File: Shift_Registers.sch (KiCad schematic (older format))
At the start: 3 parts

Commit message: Finished draft schema
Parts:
- added J1: SPARE, symbol Connector:Conn_01x03_Female
- added U17: 74HC595, symbol 74xx:74HC595
- gave numbers to parts that had none: 3
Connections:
- net 5V: now also U17.10 (~SRCLR), U17.16 (VCC)
- net BLANK: now also U17.13 (~OE)
- net GND: now also J1.3 (Pin_3), U17.8 (GND)
- net SHIFTCLK: now also U17.11 (SRCLK)
- net STORAGECLK: now also U17.12 (RCLK)
- net at U16.9 (QH'): now also U17.14 (SER)
- new net: J1.1 (Pin_1), U17.6 (QG)
- new net: J1.2 (Pin_2), U17.7 (QH)
- new net DP1: U17.15 (QA)
- new net DP2: U17.1 (QB)
- new net DP3: U17.2 (QC)
- new net DP4: U17.3 (QD)
- new net DP5: U17.4 (QE)
- new net DP6: U17.5 (QF)
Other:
- moved on the sheet: U14, U15, U16

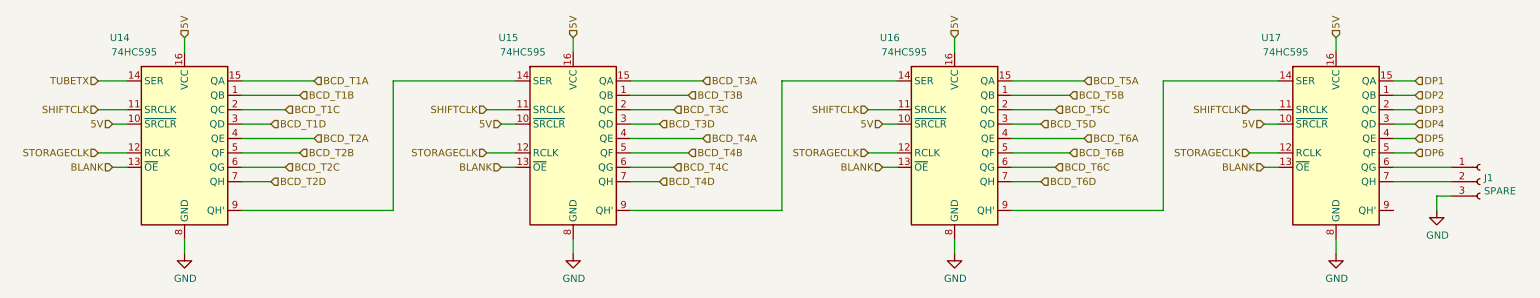
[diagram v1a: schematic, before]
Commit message: Finished schema and started PCB layout
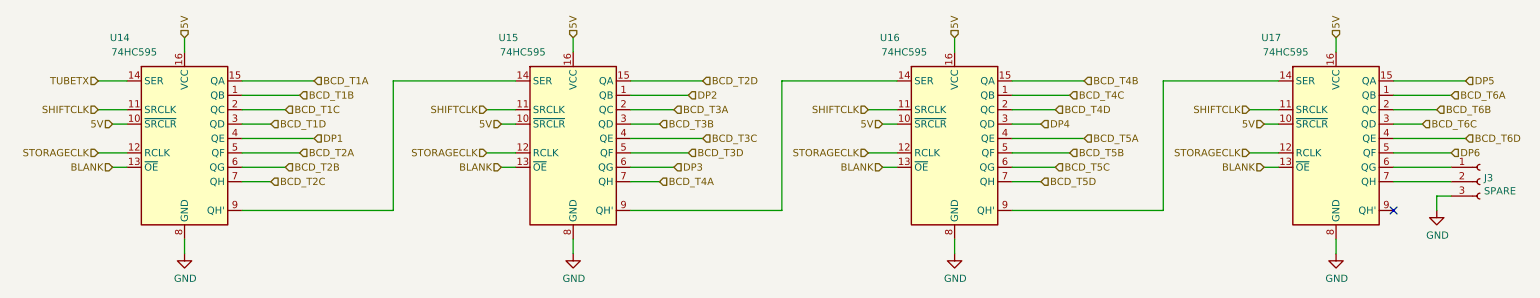
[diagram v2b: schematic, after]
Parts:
- J3: renamed from J1; footprint (none) -> Connector_PinHeader_2.54mm:PinHeader_1x03_P2.54mm_Vertical
- U14, U15, U16, U17: footprint (none) -> Package_SO:SOIC-16_3.9x9.9mm_P1.27mm
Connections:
- net BCD_T2A: now also U14.5 (QF); no longer U14.4 (QE)
- net BCD_T2B: now also U14.6 (QG); no longer U14.5 (QF)
- net BCD_T2C: now also U14.7 (QH); no longer U14.6 (QG)
- net BCD_T2D: now also U15.15 (QA); no longer U14.7 (QH)
- net BCD_T3A: now also U15.2 (QC); no longer U15.15 (QA)
- net BCD_T3B: now also U15.3 (QD); no longer U15.1 (QB)
- net BCD_T3C: now also U15.4 (QE); no longer U15.2 (QC)
- net BCD_T3D: now also U15.5 (QF); no longer U15.3 (QD)
- net BCD_T4A: now also U15.7 (QH); no longer U15.4 (QE)
- net BCD_T4B: now also U16.15 (QA); no longer U15.5 (QF)
- net BCD_T4C: now also U16.1 (QB); no longer U15.6 (QG)
- net BCD_T4D: now also U16.2 (QC); no longer U15.7 (QH)
- net BCD_T5A: now also U16.4 (QE); no longer U16.15 (QA)
- net BCD_T5B: now also U16.5 (QF); no longer U16.1 (QB)
- net BCD_T5C: now also U16.6 (QG); no longer U16.2 (QC)
- net BCD_T5D: now also U16.7 (QH); no longer U16.3 (QD)
- net BCD_T6A: now also U17.1 (QB); no longer U16.4 (QE)
- net BCD_T6B: now also U17.2 (QC); no longer U16.5 (QF)
- net BCD_T6C: now also U17.3 (QD); no longer U16.6 (QG)
- net BCD_T6D: now also U17.4 (QE); no longer U16.7 (QH)
- net DP1: now also U14.4 (QE); no longer U17.15 (QA)
- net DP2: now also U15.1 (QB); no longer U17.1 (QB)
- net DP3: now also U15.6 (QG); no longer U17.2 (QC)
- net DP4: now also U16.3 (QD); no longer U17.3 (QD)
- net DP5: now also U17.15 (QA); no longer U17.4 (QE)
- no-connect marks 0 -> 1
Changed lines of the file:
@@
 Comment4 ""
 $EndDescr
+Text HLabel 10600 3300 2    50   Input ~ 0
+BCD_T6A
+Text HLabel 10500 3400 2    50   Input ~ 0
+BCD_T6B
+Text HLabel 10400 3500 2    50   Input ~ 0
+BCD_T6C
 Text HLabel 8050 3600 2    50   Input ~ 0
-BCD_T6A
+BCD_T5A
 Text HLabel 7950 3700 2    50   Input ~ 0
-BCD_T6B
+BCD_T5B
 Text HLabel 7850 3800 2    50   Input ~ 0
-BCD_T6C
+BCD_T5C
+Text HLabel 7750 3900 2    50   Input ~ 0
+BCD_T5D
+Text HLabel 5100 3900 2    50   Input ~ 0
+BCD_T4A
 Text HLabel 8050 3200 2    50   Input ~ 0
-BCD_T5A
+BCD_T4B
 Text HLabel 7950 3300 2    50   Input ~ 0
-BCD_T5B
+BCD_T4C
 Text HLabel 7850 3400 2    50   Input ~ 0
-BCD_T5C
-Text HLabel 7750 3500 2    50   Input ~ 0
-BCD_T5D
-Text HLabel 5400 3600 2    50   Input ~ 0
-BCD_T4A
-Text HLabel 5300 3700 2    50   Input ~ 0
-BCD_T4B
-Text HLabel 5200 3800 2    50   Input ~ 0
-BCD_T4C
-Text HLabel 5100 3900 2    50   Input ~ 0
 BCD_T4D
-Text HLabel 7750 3900 2    50   Input ~ 0
+Text HLabel 10700 3600 2    50   Input ~ 0
 BCD_T6D
 Text HLabel 2500 3400 2    50   Input ~ 0
 BCD_T1C
-Text HLabel 2700 3600 2    50   Input ~ 0
+Text HLabel 2600 3700 2    50   Input ~ 0
 BCD_T2A
-Text HLabel 2500 3800 2    50   Input ~ 0
+Text HLabel 2400 3900 2    50   Input ~ 0
 BCD_T2C
-Text HLabel 5400 3200 2    50   Input ~ 0
+Text HLabel 5200 3400 2    50   Input ~ 0
 BCD_T3A
-Text HLabel 5300 3300 2    50   Input ~ 0
+Text HLabel 5100 3500 2    50   Input ~ 0
 BCD_T3B
-Text HLabel 5200 3400 2    50   Input ~ 0
+Text HLabel 5400 3600 2    50   Input ~ 0
 BCD_T3C
-Text HLabel 5100 3500 2    50   Input ~ 0
+Text HLabel 5300 3700 2    50   Input ~ 0
 BCD_T3D
 $Comp
@@
 F 0 "U14" H 1350 4300 50  0000 C CNN
 F 1 "74HC595" H 1450 4200 50  0000 C CNN
-F 2 "" H 1800 3600 50  0001 C CNN
+F 2 "Package_SO:SOIC-16_3.9x9.9mm_P1.27mm" H 1800 3600 50  0001 C CNN
 F 3 "http://www.ti.com/lit/ds/symlink/sn74hc595.pdf" H 1800 3600 50  0001 C CNN
 	1    1800 3600
@@
 Wire Wire Line
 	1300 3800 1400 3800
-Text HLabel 2400 3900 2    50   Input ~ 0
+Text HLabel 5400 3200 2    50   Input ~ 0
 BCD_T2D
-Text HLabel 2600 3700 2    50   Input ~ 0
+Text HLabel 2500 3800 2    50   Input ~ 0
 BCD_T2B
 Text HLabel 2400 3500 2    50   Input ~ 0
@@
 F 0 "U15" H 4050 4300 50  0000 C CNN
 F 1 "74HC595" H 4150 4200 50  0000 C CNN
-F 2 "" H 4500 3600 50  0001 C CNN
+F 2 "Package_SO:SOIC-16_3.9x9.9mm_P1.27mm" H 4500 3600 50  0001 C CNN
 F 3 "http://www.ti.com/lit/ds/symlink/sn74hc595.pdf" H 4500 3600 50  0001 C CNN
 	1    4500 3600
@@
 F 0 "U16" H 6700 4300 50  0000 C CNN
 F 1 "74HC595" H 6800 4200 50  0000 C CNN
-F 2 "" H 7150 3600 50  0001 C CNN
+F 2 "Package_SO:SOIC-16_3.9x9.9mm_P1.27mm" H 7150 3600 50  0001 C CNN
 F 3 "http://www.ti.com/lit/ds/symlink/sn74hc595.pdf" H 7150 3600 50  0001 C CNN
 	1    7150 3600
@@
 	1    0    0    -1
 $EndComp
-Wire Wire Line
-	7150 4400 7150 4300
 Text HLabel 6650 3800 0    50   Input ~ 0
 BLANK
@@
 F 0 "U17" H 9350 4300 50  0000 C CNN
 F 1 "74HC595" H 9450 4200 50  0000 C CNN
-F 2 "" H 9800 3600 50  0001 C CNN
+F 2 "Package_SO:SOIC-16_3.9x9.9mm_P1.27mm" H 9800 3600 50  0001 C CNN
 F 3 "http://www.ti.com/lit/ds/symlink/sn74hc595.pdf" H 9800 3600 50  0001 C CNN
 	1    9800 3600
@@
 Wire Wire Line
 	9300 3800 9400 3800
-Text HLabel 10350 3700 2    50   Input ~ 0
+Text HLabel 10600 3700 2    50   Input ~ 0
 DP6
-Text HLabel 10350 3600 2    50   Input ~ 0
+Text HLabel 10700 3200 2    50   Input ~ 0
 DP5
-Text HLabel 10350 3500 2    50   Input ~ 0
+Text HLabel 7750 3500 2    50   Input ~ 0
 DP4
-Text HLabel 10350 3400 2    50   Input ~ 0
+Text HLabel 5200 3800 2    50   Input ~ 0
 DP3
-Text HLabel 10350 3300 2    50   Input ~ 0
+Text HLabel 5300 3300 2    50   Input ~ 0
 DP2
-Text HLabel 10350 3200 2    50   Input ~ 0
+Text HLabel 2700 3600 2    50   Input ~ 0
 DP1
-Wire Wire Line
-	10200 3200 10350 3200
-Wire Wire Line
-	10200 3300 10350 3300
-Wire Wire Line
-	10350 3400 10200 3400
-Wire Wire Line
-	10200 3500 10350 3500
-Wire Wire Line
-	10350 3600 10200 3600
-Wire Wire Line
-	10350 3700 10200 3700
-$Comp
-L Connector:Conn_01x03_Female J1
+$Comp
+L Connector:Conn_01x03_Female J3
 U 1 1 5D9437D9
 P 10800 3900
-F 0 "J1" H 10828 3926 50  0000 L CNN
+F 0 "J3" H 10828 3926 50  0000 L CNN
 F 1 "SPARE" H 10828 3835 50  0000 L CNN
-F 2 "" H 10800 3900 50  0001 C CNN
+F 2 "Connector_PinHeader_2.54mm:PinHeader_1x03_P2.54mm_Vertical" H 10800 3900 50  0001 C CNN
 F 3 "~" H 10800 3900 50  0001 C CNN
 	1    10800 3900
@@
 Wire Wire Line
 	8600 3200 9400 3200
+NoConn ~ 10200 4100
+Wire Wire Line
+	7150 4300 7150 4400
+Wire Wire Line
+	10200 3600 10700 3600
+Wire Wire Line
+	10200 3700 10600 3700
+Wire Wire Line
+	10200 3500 10400 3500
+Wire Wire Line
+	10200 3400 10500 3400
+Wire Wire Line
+	10200 3300 10600 3300
+Wire Wire Line
+	10200 3200 10700 3200
 $EndSCHEMATC

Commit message: 90% routed
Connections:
- net BCD_T1A: now also U14.2 (QC); no longer U14.15 (QA)
- net BCD_T1B: now also U14.4 (QE); no longer U14.1 (QB)
- net BCD_T1C: now also U14.5 (QF); no longer U14.2 (QC)
- net BCD_T2A: now also U14.6 (QG); no longer U14.5 (QF)
- net BCD_T2B: now also U14.7 (QH); no longer U14.6 (QG)
- net BCD_T2C: now also U14.15 (QA); no longer U14.7 (QH)
- net BCD_T2D: now also U15.2 (QC); no longer U15.15 (QA)
- net BCD_T3A: now also U15.6 (QG); no longer U15.2 (QC)
- net BCD_T3B: now also U15.4 (QE); no longer U15.3 (QD)
- net BCD_T3C: now also U15.3 (QD); no longer U15.4 (QE)
- net BCD_T4A: now also U15.15 (QA); no longer U15.7 (QH)
- net BCD_T4B: now also U16.3 (QD); no longer U16.15 (QA)
- net BCD_T4C: now also U16.4 (QE); no longer U16.1 (QB)
- net BCD_T5A: now also U16.15 (QA); no longer U16.4 (QE)
- net BCD_T5B: now also U16.6 (QG); no longer U16.5 (QF)
- net BCD_T5C: now also U16.5 (QF); no longer U16.6 (QG)
- net BCD_T6A: now also U17.5 (QF); no longer U17.1 (QB)
- net BCD_T6B: now also U17.3 (QD); no longer U17.2 (QC)
- net BCD_T6C: now also U17.2 (QC); no longer U17.3 (QD)
- net DP1: now also U14.1 (QB); no longer U14.4 (QE)
- net DP3: now also U15.7 (QH); no longer U15.6 (QG)
- net DP4: now also U16.1 (QB); no longer U16.3 (QD)
- net DP5: now also U17.1 (QB); no longer U17.15 (QA)
- net DP6: now also U17.15 (QA); no longer U17.5 (QF)
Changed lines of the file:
@@
 Comment4 ""
 $EndDescr
-Text HLabel 10600 3300 2    50   Input ~ 0
+Text HLabel 10600 3700 2    50   Input ~ 0
 BCD_T6A
+Text HLabel 10400 3500 2    50   Input ~ 0
+BCD_T6B
 Text HLabel 10500 3400 2    50   Input ~ 0
-BCD_T6B
-Text HLabel 10400 3500 2    50   Input ~ 0
 BCD_T6C
-Text HLabel 8050 3600 2    50   Input ~ 0
+Text HLabel 8050 3200 2    50   Input ~ 0
 BCD_T5A
+Text HLabel 7850 3800 2    50   Input ~ 0
+BCD_T5B
 Text HLabel 7950 3700 2    50   Input ~ 0
-BCD_T5B
-Text HLabel 7850 3800 2    50   Input ~ 0
 BCD_T5C
 Text HLabel 7750 3900 2    50   Input ~ 0
 BCD_T5D
-Text HLabel 5100 3900 2    50   Input ~ 0
+Text HLabel 5400 3200 2    50   Input ~ 0
 BCD_T4A
-Text HLabel 8050 3200 2    50   Input ~ 0
+Text HLabel 7750 3500 2    50   Input ~ 0
 BCD_T4B
-Text HLabel 7950 3300 2    50   Input ~ 0
+Text HLabel 8050 3600 2    50   Input ~ 0
 BCD_T4C
 Text HLabel 7850 3400 2    50   Input ~ 0
@@
 Text HLabel 10700 3600 2    50   Input ~ 0
 BCD_T6D
-Text HLabel 2500 3400 2    50   Input ~ 0
+Text HLabel 2600 3700 2    50   Input ~ 0
 BCD_T1C
-Text HLabel 2600 3700 2    50   Input ~ 0
+Text HLabel 2500 3800 2    50   Input ~ 0
 BCD_T2A
-Text HLabel 2400 3900 2    50   Input ~ 0
+Text HLabel 2700 3200 2    50   Input ~ 0
 BCD_T2C
-Text HLabel 5200 3400 2    50   Input ~ 0
+Text HLabel 5200 3800 2    50   Input ~ 0
 BCD_T3A
+Text HLabel 5400 3600 2    50   Input ~ 0
+BCD_T3B
 Text HLabel 5100 3500 2    50   Input ~ 0
-BCD_T3B
-Text HLabel 5400 3600 2    50   Input ~ 0
 BCD_T3C
 Text HLabel 5300 3700 2    50   Input ~ 0
@@
 	1    0    0    -1
 $EndComp
-Text HLabel 2700 3200 2    50   Input ~ 0
+Text HLabel 2500 3400 2    50   Input ~ 0
 BCD_T1A
 $Comp
@@
 Wire Wire Line
 	1300 3800 1400 3800
-Text HLabel 5400 3200 2    50   Input ~ 0
+Text HLabel 5200 3400 2    50   Input ~ 0
 BCD_T2D
-Text HLabel 2500 3800 2    50   Input ~ 0
+Text HLabel 2400 3900 2    50   Input ~ 0
 BCD_T2B
 Text HLabel 2400 3500 2    50   Input ~ 0
 BCD_T1D
-Text HLabel 2600 3300 2    50   Input ~ 0
+Text HLabel 2700 3600 2    50   Input ~ 0
 BCD_T1B
 Wire Wire Line
@@
 Wire Wire Line
 	9300 3800 9400 3800
-Text HLabel 10600 3700 2    50   Input ~ 0
+Text HLabel 10700 3200 2    50   Input ~ 0
 DP6
-Text HLabel 10700 3200 2    50   Input ~ 0
+Text HLabel 10600 3300 2    50   Input ~ 0
 DP5
-Text HLabel 7750 3500 2    50   Input ~ 0
+Text HLabel 7950 3300 2    50   Input ~ 0
 DP4
-Text HLabel 5200 3800 2    50   Input ~ 0
+Text HLabel 5100 3900 2    50   Input ~ 0
 DP3
 Text HLabel 5300 3300 2    50   Input ~ 0
 DP2
-Text HLabel 2700 3600 2    50   Input ~ 0
+Text HLabel 2600 3300 2    50   Input ~ 0
 DP1
 $Comp

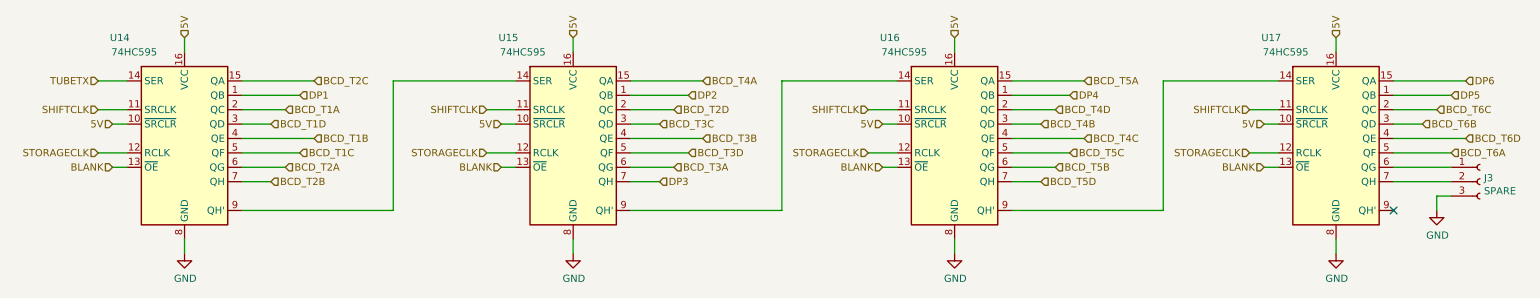
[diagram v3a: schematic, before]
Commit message: Completed layout inc optimisation of data pattern for shift registers
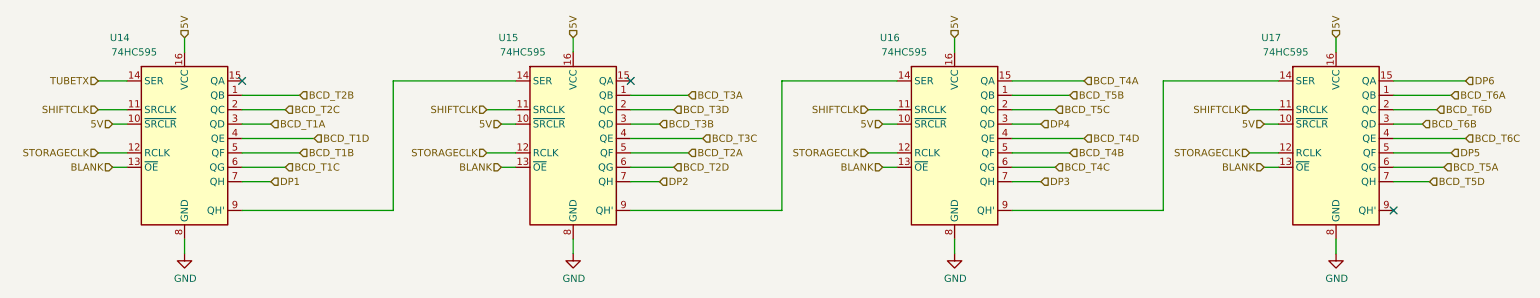
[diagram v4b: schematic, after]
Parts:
- removed J3: SPARE, Connector_PinHeader_2.54mm:PinHeader_1x03_P2.54mm_Vertical, symbol Connector:Conn_01x03_Female
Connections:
- net BCD_T1A: now also U14.3 (QD); no longer U14.2 (QC)
- net BCD_T1B: now also U14.5 (QF); no longer U14.4 (QE)
- net BCD_T1C: now also U14.6 (QG); no longer U14.5 (QF)
- net BCD_T1D: now also U14.4 (QE); no longer U14.3 (QD)
- net BCD_T2A: now also U15.5 (QF); no longer U14.6 (QG)
- net BCD_T2B: now also U14.1 (QB); no longer U14.7 (QH)
- net BCD_T2C: now also U14.2 (QC); no longer U14.15 (QA)
- net BCD_T2D: now also U15.6 (QG); no longer U15.2 (QC)
- net BCD_T3A: now also U15.1 (QB); no longer U15.6 (QG)
- net BCD_T3B: now also U15.3 (QD); no longer U15.4 (QE)
- net BCD_T3C: now also U15.4 (QE); no longer U15.3 (QD)
- net BCD_T3D: now also U15.2 (QC); no longer U15.5 (QF)
- net BCD_T4A: now also U16.15 (QA); no longer U15.15 (QA)
- net BCD_T4B: now also U16.5 (QF); no longer U16.3 (QD)
- net BCD_T4C: now also U16.6 (QG); no longer U16.4 (QE)
- net BCD_T4D: now also U16.4 (QE); no longer U16.2 (QC)
- net BCD_T5A: now also U17.6 (QG); no longer U16.15 (QA)
- net BCD_T5B: now also U16.1 (QB); no longer U16.6 (QG)
- net BCD_T5C: now also U16.2 (QC); no longer U16.5 (QF)
- net BCD_T5D: now also U17.7 (QH); no longer U16.7 (QH)
- net BCD_T6A: now also U17.1 (QB); no longer U17.5 (QF)
- net BCD_T6C: now also U17.4 (QE); no longer U17.2 (QC)
- net BCD_T6D: now also U17.2 (QC); no longer U17.4 (QE)
- net DP1: now also U14.7 (QH); no longer U14.1 (QB)
- net DP2: now also U15.7 (QH); no longer U15.1 (QB)
- net DP3: now also U16.7 (QH); no longer U15.7 (QH)
- net DP4: now also U16.3 (QD); no longer U16.1 (QB)
- net DP5: now also U17.5 (QF); no longer U17.1 (QB)
- no-connect marks 1 -> 3
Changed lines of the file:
@@
 Comment4 ""
 $EndDescr
-Text HLabel 10600 3700 2    50   Input ~ 0
+Text HLabel 10600 3300 2    50   Input ~ 0
 BCD_T6A
 Text HLabel 10400 3500 2    50   Input ~ 0
 BCD_T6B
+Text HLabel 10700 3600 2    50   Input ~ 0
+BCD_T6C
 Text HLabel 10500 3400 2    50   Input ~ 0
-BCD_T6C
-Text HLabel 8050 3200 2    50   Input ~ 0
-BCD_T5A
-Text HLabel 7850 3800 2    50   Input ~ 0
-BCD_T5B
-Text HLabel 7950 3700 2    50   Input ~ 0
-BCD_T5C
-Text HLabel 7750 3900 2    50   Input ~ 0
-BCD_T5D
-Text HLabel 5400 3200 2    50   Input ~ 0
-BCD_T4A
-Text HLabel 7750 3500 2    50   Input ~ 0
-BCD_T4B
-Text HLabel 8050 3600 2    50   Input ~ 0
-BCD_T4C
-Text HLabel 7850 3400 2    50   Input ~ 0
-BCD_T4D
-Text HLabel 10700 3600 2    50   Input ~ 0
 BCD_T6D
-Text HLabel 2600 3700 2    50   Input ~ 0
+Text HLabel 2500 3800 2    50   Input ~ 0
 BCD_T1C
-Text HLabel 2500 3800 2    50   Input ~ 0
+Text HLabel 5300 3700 2    50   Input ~ 0
 BCD_T2A
-Text HLabel 2700 3200 2    50   Input ~ 0
+Text HLabel 2500 3400 2    50   Input ~ 0
 BCD_T2C
-Text HLabel 5200 3800 2    50   Input ~ 0
+Text HLabel 5300 3300 2    50   Input ~ 0
 BCD_T3A
+Text HLabel 5100 3500 2    50   Input ~ 0
+BCD_T3B
 Text HLabel 5400 3600 2    50   Input ~ 0
-BCD_T3B
-Text HLabel 5100 3500 2    50   Input ~ 0
 BCD_T3C
-Text HLabel 5300 3700 2    50   Input ~ 0
+Text HLabel 5200 3400 2    50   Input ~ 0
 BCD_T3D
 $Comp
@@
 	1    0    0    -1
 $EndComp
-Text HLabel 2500 3400 2    50   Input ~ 0
+Text HLabel 2400 3500 2    50   Input ~ 0
 BCD_T1A
 $Comp
@@
 Wire Wire Line
 	1300 3800 1400 3800
-Text HLabel 5200 3400 2    50   Input ~ 0
+Text HLabel 5200 3800 2    50   Input ~ 0
 BCD_T2D
-Text HLabel 2400 3900 2    50   Input ~ 0
+Text HLabel 2600 3300 2    50   Input ~ 0
 BCD_T2B
-Text HLabel 2400 3500 2    50   Input ~ 0
+Text HLabel 2700 3600 2    50   Input ~ 0
 BCD_T1D
-Text HLabel 2700 3600 2    50   Input ~ 0
+Text HLabel 2600 3700 2    50   Input ~ 0
 BCD_T1B
 Wire Wire Line
@@
 Wire Wire Line
 	2200 3300 2600 3300
-Wire Wire Line
-	2200 3200 2700 3200
 $Comp
 L 74xx:74HC595 U15
@@
 Wire Wire Line
 	4900 3300 5300 3300
-Wire Wire Line
-	4900 3200 5400 3200
 $Comp
 L 74xx:74HC595 U16
@@
 Wire Wire Line
 	7550 3300 7950 3300
-Wire Wire Line
-	7550 3200 8050 3200
 $Comp
 L 74xx:74HC595 U17
@@
 Text HLabel 10700 3200 2    50   Input ~ 0
 DP6
-Text HLabel 10600 3300 2    50   Input ~ 0
+Text HLabel 10600 3700 2    50   Input ~ 0
 DP5
-Text HLabel 7950 3300 2    50   Input ~ 0
-DP4
 Text HLabel 5100 3900 2    50   Input ~ 0
-DP3
-Text HLabel 5300 3300 2    50   Input ~ 0
 DP2
-Text HLabel 2600 3300 2    50   Input ~ 0
+Text HLabel 2400 3900 2    50   Input ~ 0
 DP1
-$Comp
-L Connector:Conn_01x03_Female J3
-U 1 1 5D9437D9
-P 10800 3900
-F 0 "J3" H 10828 3926 50  0000 L CNN
-F 1 "SPARE" H 10828 3835 50  0000 L CNN
-F 2 "Connector_PinHeader_2.54mm:PinHeader_1x03_P2.54mm_Vertical" H 10800 3900 50  0001 C CNN
-F 3 "~" H 10800 3900 50  0001 C CNN
-	1    10800 3900
-	1    0    0    -1
-$EndComp
-Wire Wire Line
-	10200 3800 10600 3800
-Wire Wire Line
-	10200 3900 10600 3900
-$Comp
-L power:GND #PWR020
-U 1 1 5D946805
-P 10500 4100
-F 0 "#PWR020" H 10500 3850 50  0001 C CNN
-F 1 "GND" H 10505 3927 50  0000 C CNN
-F 2 "" H 10500 4100 50  0001 C CNN
-F 3 "" H 10500 4100 50  0001 C CNN
-	1    10500 4100
-	1    0    0    -1
-$EndComp
-Wire Wire Line
-	10500 4100 10500 4000
-Wire Wire Line
-	10500 4000 10600 4000
 Wire Wire Line
 	3250 4100 3250 3200
@@
 Wire Wire Line
 	10200 3200 10700 3200
+NoConn ~ 2200 3200
+NoConn ~ 4900 3200
+Text HLabel 7750 3500 2    50   Input ~ 0
+DP4
+Text HLabel 8050 3600 2    50   Input ~ 0
+BCD_T4D
+Text HLabel 7850 3800 2    50   Input ~ 0
+BCD_T4C
+Text HLabel 7950 3700 2    50   Input ~ 0
+BCD_T4B
+Text HLabel 7850 3400 2    50   Input ~ 0
+BCD_T5C
+Text HLabel 10450 3900 2    50   Input ~ 0
+BCD_T5D
+Text HLabel 7950 3300 2    50   Input ~ 0
+BCD_T5B
+Text HLabel 10550 3800 2    50   Input ~ 0
+BCD_T5A
+Text HLabel 8050 3200 2    50   Input ~ 0
+BCD_T4A
+Text HLabel 7750 3900 2    50   Input ~ 0
+DP3
+Wire Wire Line
+	7550 3200 8050 3200
+Wire Wire Line
+	10200 3800 10550 3800
+Wire Wire Line
+	10450 3900 10200 3900
 $EndSCHEMATC

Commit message: Szitched to DIP shift registers, added BME280
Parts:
- U14, U15, U16, U17: footprint Package_SO:SOIC-16_3.9x9.9mm_P1.27mm -> Package_DIP:DIP-16_W7.62mm
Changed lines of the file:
@@
 F 0 "U14" H 1350 4300 50  0000 C CNN
 F 1 "74HC595" H 1450 4200 50  0000 C CNN
-F 2 "Package_SO:SOIC-16_3.9x9.9mm_P1.27mm" H 1800 3600 50  0001 C CNN
+F 2 "Package_DIP:DIP-16_W7.62mm" H 1800 3600 50  0001 C CNN
 F 3 "http://www.ti.com/lit/ds/symlink/sn74hc595.pdf" H 1800 3600 50  0001 C CNN
 	1    1800 3600
@@
 F 0 "U15" H 4050 4300 50  0000 C CNN
 F 1 "74HC595" H 4150 4200 50  0000 C CNN
-F 2 "Package_SO:SOIC-16_3.9x9.9mm_P1.27mm" H 4500 3600 50  0001 C CNN
+F 2 "Package_DIP:DIP-16_W7.62mm" H 4500 3600 50  0001 C CNN
 F 3 "http://www.ti.com/lit/ds/symlink/sn74hc595.pdf" H 4500 3600 50  0001 C CNN
 	1    4500 3600
@@
 F 0 "U16" H 6700 4300 50  0000 C CNN
 F 1 "74HC595" H 6800 4200 50  0000 C CNN
-F 2 "Package_SO:SOIC-16_3.9x9.9mm_P1.27mm" H 7150 3600 50  0001 C CNN
+F 2 "Package_DIP:DIP-16_W7.62mm" H 7150 3600 50  0001 C CNN
 F 3 "http://www.ti.com/lit/ds/symlink/sn74hc595.pdf" H 7150 3600 50  0001 C CNN
 	1    7150 3600
@@
 F 0 "U17" H 9350 4300 50  0000 C CNN
 F 1 "74HC595" H 9450 4200 50  0000 C CNN
-F 2 "Package_SO:SOIC-16_3.9x9.9mm_P1.27mm" H 9800 3600 50  0001 C CNN
+F 2 "Package_DIP:DIP-16_W7.62mm" H 9800 3600 50  0001 C CNN
 F 3 "http://www.ti.com/lit/ds/symlink/sn74hc595.pdf" H 9800 3600 50  0001 C CNN
 	1    9800 3600
